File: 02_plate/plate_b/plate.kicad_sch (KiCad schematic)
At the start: 67 parts, among them U1 HOLE, U10 HOLE, U11 HOLE, U12 HOLE, U13 HOLE, U14 HOLE, U15 HOLE, U16 HOLE, U17 HOLE, U18 HOLE, U19 HOLE, U2 HOLE, U20 HOLE, U21 HOLE, U22 HOLE, U23 HOLE, U24 HOLE, U25 HOLE, U26 HOLE, U27 HOLE, U28 HOLE, U29 HOLE, U3 HOLE, U30 HOLE, U31 HOLE, U32 HOLE, U33 HOLE, U34 HOLE, U35 HOLE, U36 HOLE, U37 HOLE, U38 HOLE, U39 HOLE, U4 HOLE, U40 HOLE, U41 HOLE, U42 HOLE, U43 HOLE, U44 HOLE, U45 HOLE, U46 HOLE, U47 HOLE, U48 HOLE, U49 HOLE, U5 HOLE, U50 HOLE, U51 HOLE, U52 HOLE, U6 HOLE, U7 HOLE, U8 HOLE, U9 HOLE

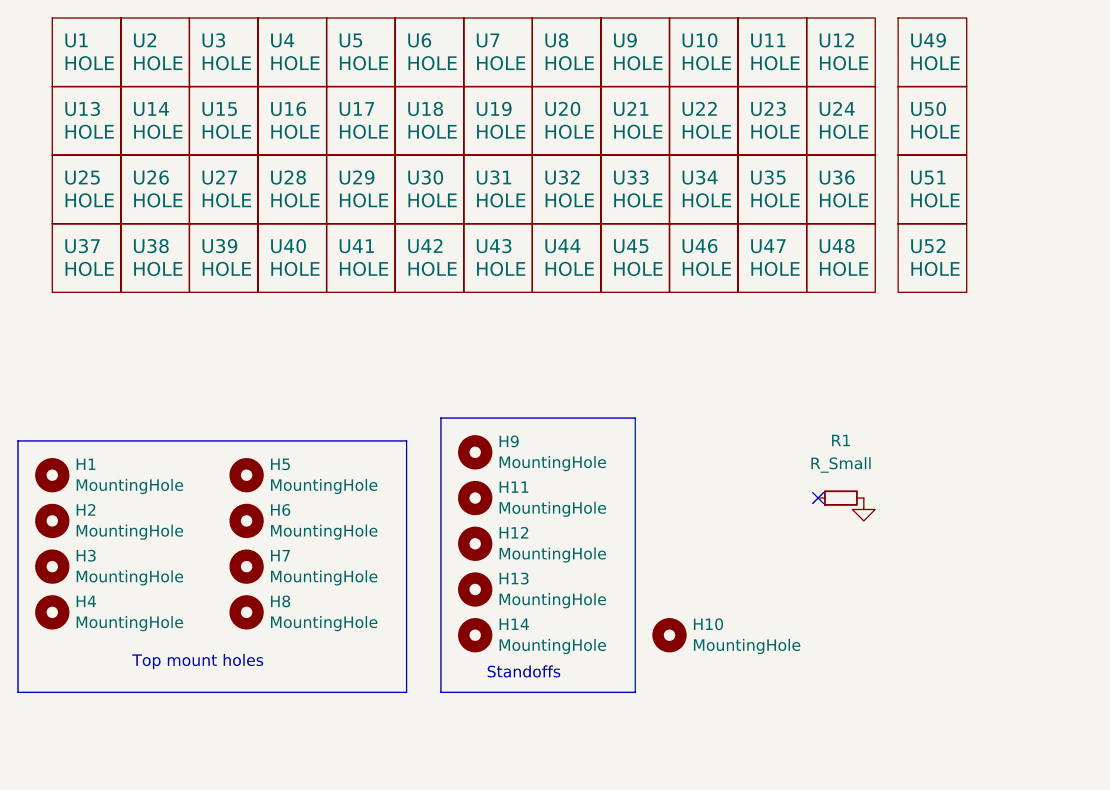
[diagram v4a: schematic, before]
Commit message: remove flex cuts, move mounting points
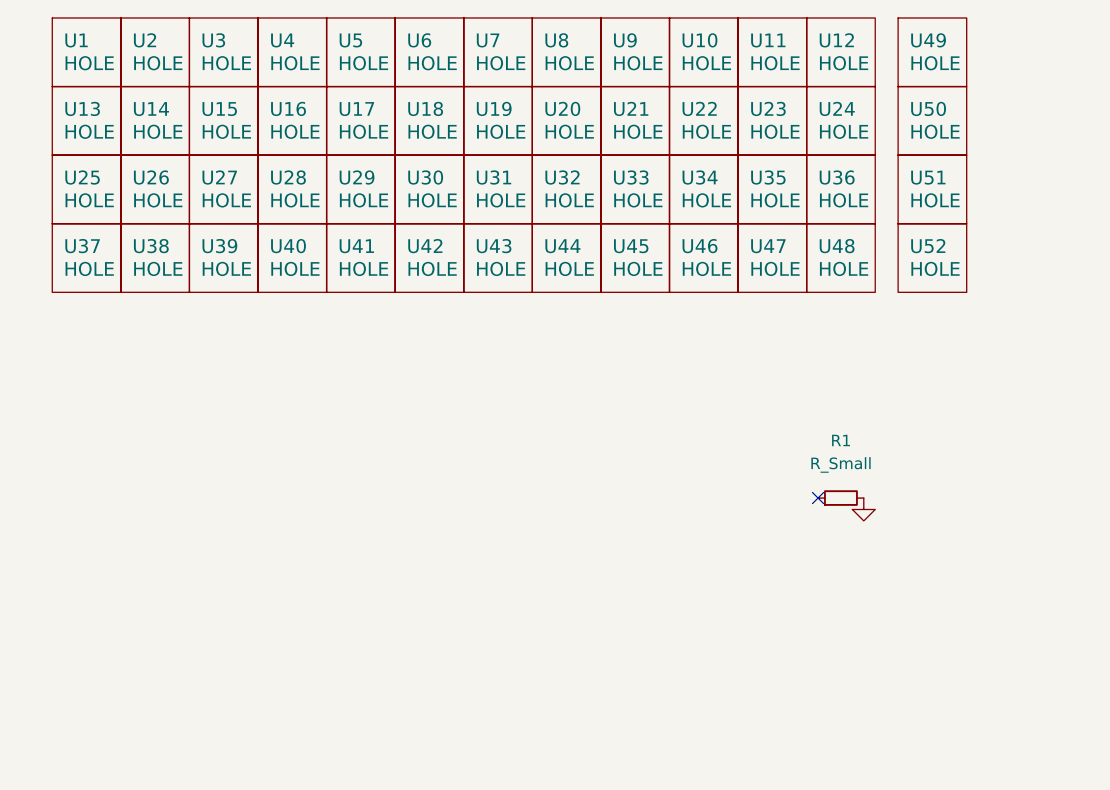
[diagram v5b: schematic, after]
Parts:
- removed H1, H2, H3, H4, H5, H6, H7, H8: MountingHole, MountingHole:MountingHole_2.2mm_M2_DIN965_Pad, symbol Mechanical:MountingHole
- removed H10, H11, H12, H13, H14, H9: MountingHole, MountingHole:MountingHole_2.2mm_M2, symbol Mechanical:MountingHole
- U48: footprint Keeb_footprints:MX100_cutout -> Keeb_footprints:MX_100_cutout
- U49, U52: footprint Keeb_footprints:EC11_cutout -> Keeb_footprints:MX_100_cutout
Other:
- note removed: "Standoffs"
- note removed: "Top mount holes"
